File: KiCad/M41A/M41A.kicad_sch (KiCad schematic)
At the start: 18 parts, among them SW1 RotaryEncoder_Switch, SW2 Rifle Fire, SW3 Granade fire, SW4 Cock, SW5 Magazine reload

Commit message: Actrualized KiCad project library.
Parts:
- removed H6: +5V, Connector_PinHeader_1.00mm:PinHeader_1x01_P1.00mm_Vertical, symbol Mechanical:MountingHole_Pad
- removed H7: GND, Connector_PinHeader_1.00mm:PinHeader_1x01_P1.00mm_Vertical, symbol Mechanical:MountingHole_Pad
- added BAT1: 5V, ProjectLibrary:Battery, symbol Device:Battery_Cell
- C1: footprint Capacitor_THT:CP_Axial_L11.0mm_D5.0mm_P18.00mm_Horizontal -> Capacitor_THT:C_Disc_D3.0mm_W2.0mm_P2.50mm
- DFPlayer1: value DFR0299 -> DFPlayer; symbol ByPS_Library:DFR0299 -> Project_Library:DFPlayer
- DRV-74HC595-1: footprint Connector_PinHeader_1.00mm:PinHeader_1x03_P1.00mm_Vertical -> Connector_PinHeader_1.00mm:PinHeader_1x05_P1.00mm_Vertical; symbol ByPS_Library:Driver-74HC595-2 -> Project_Library:Driver-74HC595-2
- LS1: footprint Connector_PinHeader_1.00mm:PinHeader_1x02_P1.00mm_Vertical -> ProjectLibrary:Speaker
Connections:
- net GND: now also SW1.C, BAT1.2 (-); no longer SW1.5 (GND)
- net at DRV-74HC595-1.1 (VCC): now also A1.14 (D11)
- net at DRV-74HC595-1.2 (GND): now also A1.15 (D12)
- net at DRV-74HC595-1.3 (SDD): now also A1.16 (D13)
- net at DRV-74HC595-1.5 (LOAD): now also A1.27 (+5V), D1.2 (A), SW1.S2, BAT1.1 (+)
- net at A1.12 (D9): now also SW1.A; no longer SW1.1 (S1)
- net at A1.13 (D10): now also SW1.B; no longer SW1.2 (S2)
- net at A1.20 (A1): now also SW1.S1; no longer SW1.3 (KEY)
- removed net +5V: A1.27 (+5V), D1.2 (A), DRV-74HC595-1.5 (LOAD), SW1.4 (5V)

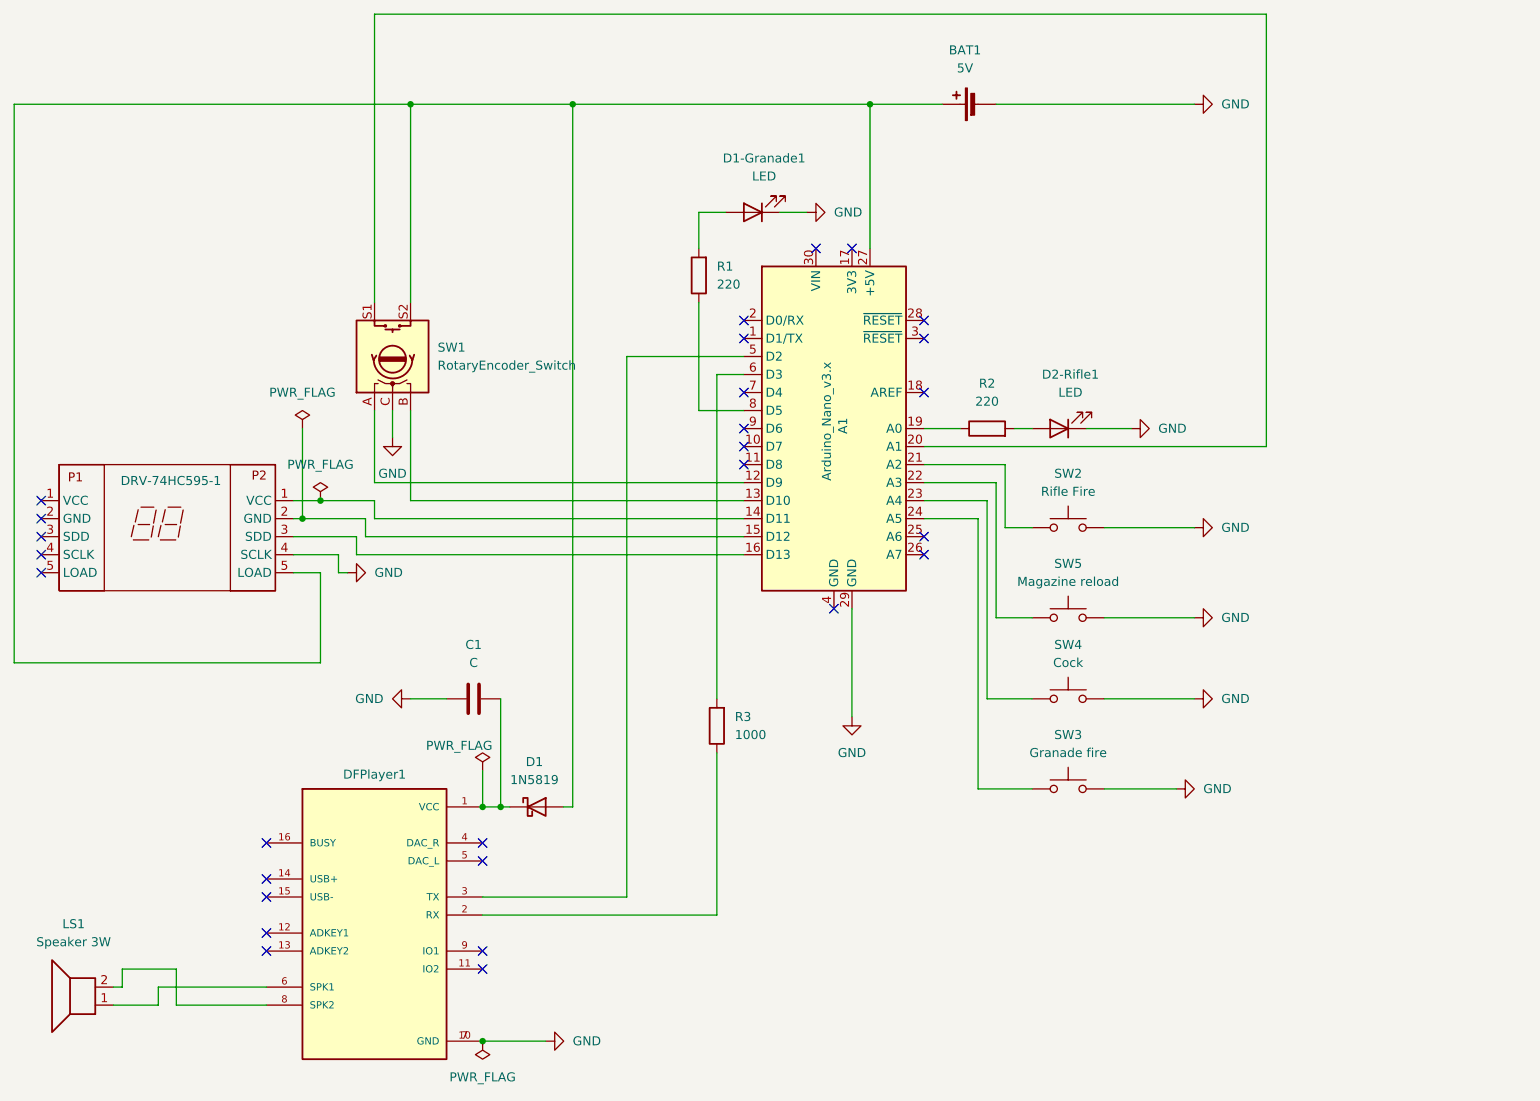
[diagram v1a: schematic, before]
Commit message: Little chage in connection to key pin of rotary encoder.
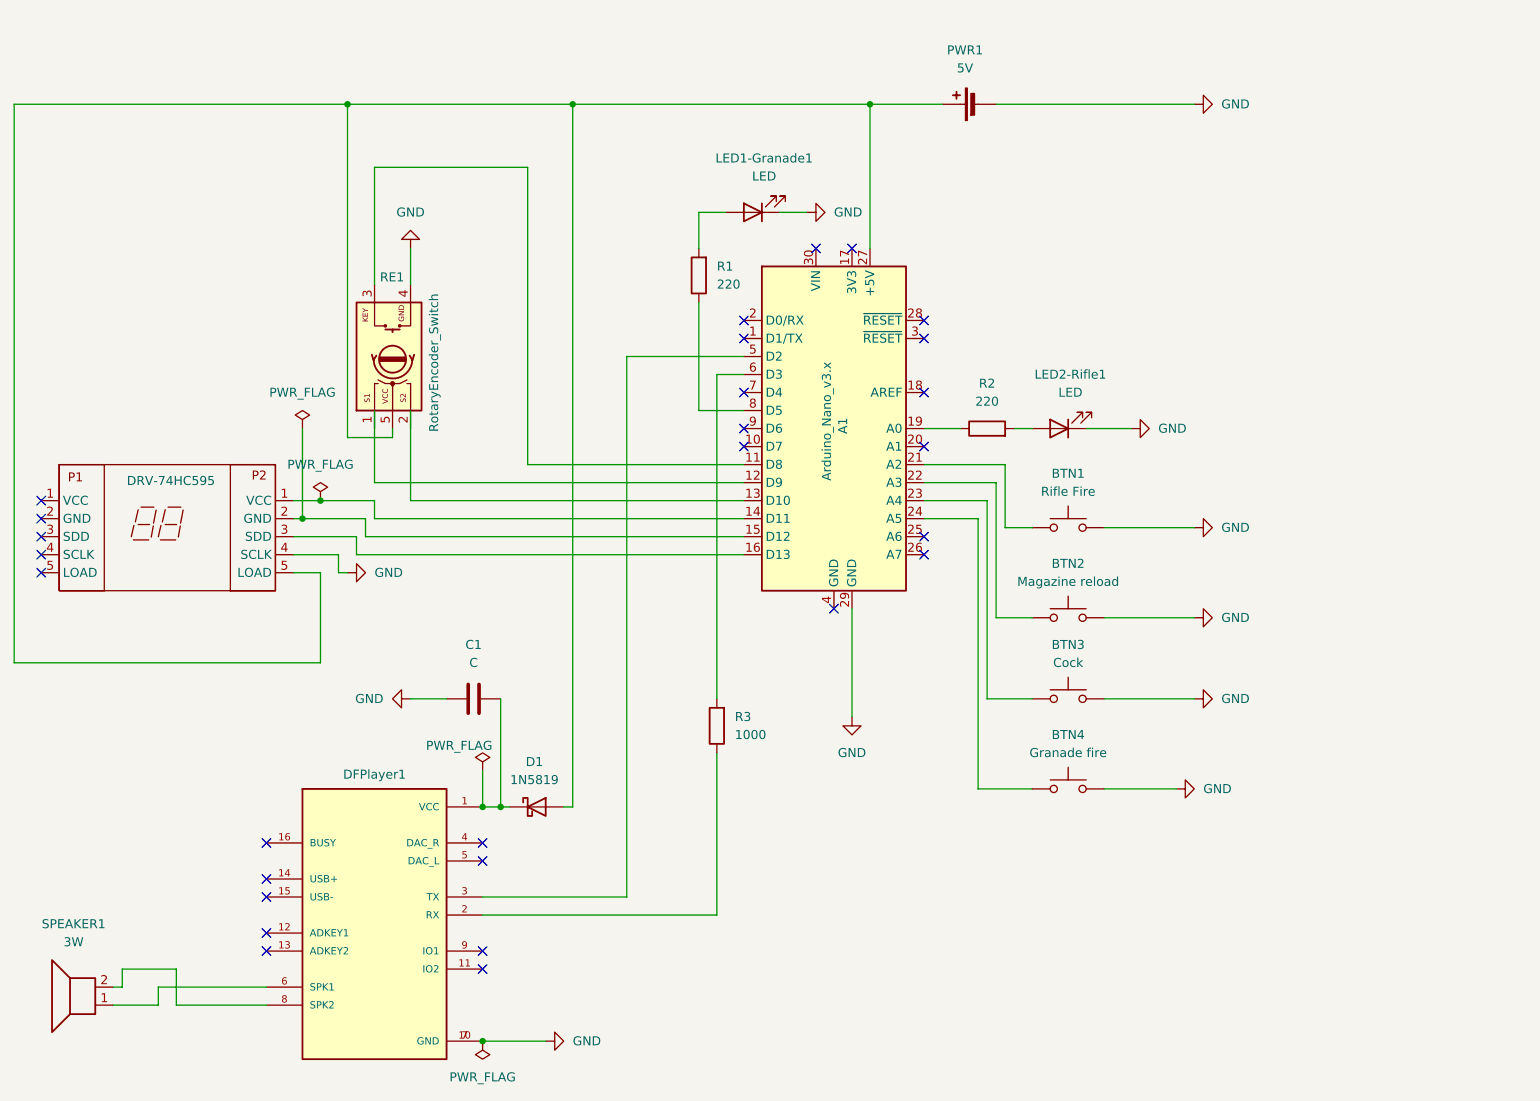
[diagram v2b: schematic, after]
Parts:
- RE1: renamed from SW1; footprint Connector_PinHeader_1.00mm:PinHeader_1x03_P1.00mm_Vertical -> ProjectLibrary:RotaryEncoderLeads; symbol Device:RotaryEncoder_Switch -> Project_Library:RotaryEncoder_Switch
- SPEAKER1: renamed from LS1; value Speaker 3W -> 3W
- renumbered SW2 to BTN1, SW5 to BTN2, SW4 to BTN3, SW3 to BTN4, DRV-74HC595-1 to DRV-74HC595, D1-Granade1 to LED1-Granade1, D2-Rifle1 to LED2-Rifle1, BAT1 to PWR1
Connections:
- net GND: now also RE1.4 (GND); no longer RE1.C
- net at DRV-74HC595.1 (VCC): now also A1.14 (D11)
- net at DRV-74HC595.2 (GND): now also A1.15 (D12)
- net at DRV-74HC595.3 (SDD): now also A1.16 (D13)
- net at DRV-74HC595.5 (LOAD): now also A1.27 (+5V), D1.2 (A), PWR1.1 (+), RE1.5 (VCC)
- net at A1.12 (D9): no longer RE1.A
- net at A1.13 (D10): no longer RE1.B
- net at A1.20 (A1): no longer RE1.S1
- net at A1.11 (D8): now also RE1.3 (KEY)
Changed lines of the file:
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@@
-	)
-	(junction
-		(at 71.12 34.29)
-		(diameter 0)
-		(color 0 0 0 0)
 	)
 	(junction
@@
 	)
 	(junction
+		(at 62.23 34.29)
+		(diameter 0)
+		(color 0 0 0 0)
+	)
+	(junction
 		(at 58.42 90.17)
 		(diameter 0)
@@
 	)
 	(no_connect
+		(at 143.51 82.55)
+	)
+	(no_connect
 		(at 50.8 138.43)
 	)
@@
 	)
 	(no_connect
-		(at 118.11 85.09)
-	)
-	(no_connect
 		(at 128.27 54.61)
 	)
@@
 	(wire
 		(pts
+			(xy 87.63 43.18) (xy 87.63 85.09)
+		)
+		(stroke
+			(width 0)
+			(type default)
+		)
+	)
+	(wire
+		(pts
 			(xy 151.13 130.81) (xy 151.13 92.71)
 		)
@@
 	(wire
 		(pts
+			(xy 62.23 34.29) (xy 93.98 34.29)
+		)
+		(stroke
+			(width 0)
+			(type default)
+		)
+	)
+	(wire
+		(pts
 			(xy 114.3 72.39) (xy 114.3 118.11)
 		)
@@
 	(wire
 		(pts
-			(xy 68.58 77.47) (xy 68.58 81.28)
-		)
-		(stroke
-			(width 0)
-			(type default)
-		)
-	)
-	(wire
-		(pts
 			(xy 63.5 95.25) (xy 54.61 95.25)
 		)
@@
 	(wire
 		(pts
-			(xy 143.51 82.55) (xy 191.77 82.55)
-		)
-		(stroke
-			(width 0)
-			(type default)
-		)
-	)
-	(wire
-		(pts
 			(xy 66.04 77.47) (xy 66.04 87.63)
 		)
@@
 	(wire
 		(pts
-			(xy 66.04 21.59) (xy 191.77 21.59)
+			(xy 66.04 59.69) (xy 66.04 43.18)
 		)
 		(stroke
@@
 	(wire
 		(pts
-			(xy 66.04 21.59) (xy 66.04 62.23)
-		)
-		(stroke
-			(width 0)
-			(type default)
-		)
-	)
-	(wire
-		(pts
-			(xy 15.24 34.29) (xy 71.12 34.29)
+			(xy 15.24 34.29) (xy 62.23 34.29)
 		)
 		(stroke
@@
 	(wire
 		(pts
+			(xy 68.58 80.01) (xy 68.58 81.28)
+		)
+		(stroke
+			(width 0)
+			(type default)
+		)
+	)
+	(wire
+		(pts
 			(xy 154.94 93.98) (xy 158.75 93.98)
 		)
@@
 	(wire
 		(pts
-			(xy 191.77 82.55) (xy 191.77 21.59)
-		)
-		(stroke
-			(width 0)
-			(type default)
-		)
-	)
-	(wire
-		(pts
-			(xy 71.12 34.29) (xy 71.12 62.23)
+			(xy 87.63 85.09) (xy 118.11 85.09)
 		)
 		(stroke
@@
 	(wire
 		(pts
+			(xy 62.23 81.28) (xy 62.23 34.29)
+		)
+		(stroke
+			(width 0)
+			(type default)
+		)
+	)
+	(wire
+		(pts
 			(xy 118.11 69.85) (xy 101.6 69.85)
 		)
@@
 	(wire
 		(pts
-			(xy 71.12 34.29) (xy 93.98 34.29)
-		)
-		(stroke
-			(width 0)
-			(type default)
-		)
-	)
-	(wire
-		(pts
 			(xy 135.89 34.29) (xy 135.89 54.61)
 		)
@@
 	(wire
 		(pts
+			(xy 66.04 43.18) (xy 87.63 43.18)
+		)
+		(stroke
+			(width 0)
+			(type default)
+		)
+	)
+	(wire
+		(pts
 			(xy 168.91 93.98) (xy 181.61 93.98)
 		)
@@
 		(pts
 			(xy 111.76 62.23) (xy 111.76 77.47)
+		)
+		(stroke
+			(width 0)
+			(type default)
+		)
+	)
+	(wire
+		(pts
+			(xy 71.12 54.61) (xy 71.12 59.69)
+		)
+		(stroke
+			(width 0)
+			(type default)
+		)
+	)
+	(wire
+		(pts
+			(xy 68.58 81.28) (xy 62.23 81.28)
 		)
 		(stroke
@@
 		(dnp no)
 		(fields_autoplaced yes)
-		(property "Reference" "SW4"
+		(property "Reference" "BTN3"
 			(at 163.83 110.49 0)
 			(effects
@@
 			(project "M41A"
 				(path "/acff4d07-702e-487a-b98e-cf041378c177"
-					(reference "SW4")
+					(reference "BTN3")
 					(unit 1)
 				)
@@
 		(dnp no)
 		(fields_autoplaced yes)
-		(property "Reference" "LS1"
+		(property "Reference" "SPEAKER1"
 			(at 23.622 149.86 0)
 			(effects
@@
 			)
 		)
-		(property "Value" "Speaker 3W"
+		(property "Value" "3W"
 			(at 23.622 152.4 0)
 			(effects
@@
 			(project "M41A"
 				(path "/acff4d07-702e-487a-b98e-cf041378c177"
-					(reference "LS1")
+					(reference "SPEAKER1")
 					(unit 1)
 				)
@@
 		(on_board yes)
 		(dnp no)
-		(property "Reference" "DRV-74HC595-1"
+		(property "Reference" "DRV-74HC595"
 			(at 37.338 87.376 0)
 			(effects
@@
 			(project "M41A"
 				(path "/acff4d07-702e-487a-b98e-cf041378c177"
-					(reference "DRV-74HC595-1")
+					(reference "DRV-74HC595")
 					(unit 1)
 				)
@@
 	(symbol
 		(lib_id "power:GND")
-		(at 68.58 81.28 0)
+		(at 71.12 54.61 180)
 		(unit 1)
 		(exclude_from_sim no)
@@
 		(fields_autoplaced yes)
 		(property "Reference" "#PWR06"
-			(at 68.58 87.63 0)
+			(at 71.12 48.26 0)
 			(effects
 				(font
@@
 		)
 		(property "Value" "GND"
-			(at 68.58 86.36 0)
+			(at 71.12 49.53 0)
 			(effects
 				(font
@@
 		)
 		(property "Footprint" ""
-			(at 68.58 81.28 0)
+			(at 71.12 54.61 0)
 			(effects
 				(font
@@
 		)
 		(property "Datasheet" ""
-			(at 68.58 81.28 0)
+			(at 71.12 54.61 0)
 			(effects
 				(font
@@
 		)
 		(property "Description" "Power symbol creates a global label with name \"GND\" , ground"
-			(at 68.58 81.28 0)
+			(at 71.12 54.61 0)
 			(effects
 				(font
@@
 		(dnp no)
 		(fields_autoplaced yes)
-		(property "Reference" "D1-Granade1"
+		(property "Reference" "LED1-Granade1"
 			(at 120.9675 41.91 0)
 			(effects
@@
 			(project "M41A"
 				(path "/acff4d07-702e-487a-b98e-cf041378c177"
-					(reference "D1-Granade1")
+					(reference "LED1-Granade1")
 					(unit 1)
 				)
@@
 		(on_board yes)
 		(dnp no)
-		(property "Reference" "SW2"
+		(property "Reference" "BTN1"
 			(at 163.83 86.36 0)
 			(effects
@@
 			(project "M41A"
 				(path "/acff4d07-702e-487a-b98e-cf041378c177"
-					(reference "SW2")
+					(reference "BTN1")
 					(unit 1)
 				)
@@
 	)
 	(symbol
-		(lib_id "Device:RotaryEncoder_Switch")
+		(lib_id "Project_Library:RotaryEncoder_Switch")
 		(at 68.58 69.85 90)
 		(unit 1)
@@
 		(on_board yes)
 		(dnp no)
-		(fields_autoplaced yes)
-		(property "Reference" "SW1"
-			(at 74.93 68.5799 90)
+		(property "Reference" "RE1"
+			(at 66.802 58.674 90)
 			(effects
 				(font
@@
 		)
 		(property "Value" "RotaryEncoder_Switch"
-			(at 74.93 71.1199 90)
+			(at 74.422 60.96 0)
 			(effects
 				(font
@@
 			)
 		)
-		(property "Footprint" "Connector_PinHeader_1.00mm:PinHeader_1x03_P1.00mm_Vertical"
-			(at 58.674 71.628 0)
+		(property "Footprint" "ProjectLibrary:RotaryEncoderLeads"
+			(at 48.768 69.596 0)
 			(effects
 				(font
@@
 		)
 		(property "Description" "Rotary encoder, dual channel, incremental quadrate outputs, with switch"
-			(at 81.026 68.072 0)
-			(effects
-				(font
-					(size 1.27 1.27)
-				)
-				(hide yes)
-			)
-		)
-		(pin "S1"
-		)
-		(pin "C"
-		)
-		(pin "B"
-		)
-		(pin "S2"
-		)
-		(pin "A"
+			(at 87.376 67.31 0)
+			(effects
+				(font
+					(size 1.27 1.27)
+				)
+				(hide yes)
+			)
+		)
+		(pin "4"
+		)
+		(pin "3"
+		)
+		(pin "2"
+		)
+		(pin "5"
+		)
+		(pin "1"
 		)
 		(instances
 			(project "M41A"
 				(path "/acff4d07-702e-487a-b98e-cf041378c177"
-					(reference "SW1")
+					(reference "RE1")
 					(unit 1)
 				)
@@
 		(dnp no)
 		(fields_autoplaced yes)
-		(property "Reference" "D2-Rifle1"
+		(property "Reference" "LED2-Rifle1"
 			(at 164.1475 72.39 0)
 			(effects
@@
 			(project "M41A"
 				(path "/acff4d07-702e-487a-b98e-cf041378c177"
-					(reference "D2-Rifle1")
+					(reference "LED2-Rifle1")
 					(unit 1)
 				)
@@
 		(dnp no)
 		(fields_autoplaced yes)
-		(property "Reference" "BAT1"
+		(property "Reference" "PWR1"
 			(at 149.2885 26.67 90)
 			(effects
@@
 			(project "M41A"
 				(path "/acff4d07-702e-487a-b98e-cf041378c177"
-					(reference "BAT1")
+					(reference "PWR1")
 					(unit 1)
 				)
@@
 		(dnp no)
 		(fields_autoplaced yes)
-		(property "Reference" "SW5"
+		(property "Reference" "BTN2"
 			(at 163.83 99.06 0)
 			(effects
@@
 			(project "M41A"
 				(path "/acff4d07-702e-487a-b98e-cf041378c177"
-					(reference "SW5")
+					(reference "BTN2")
 					(unit 1)
 				)
@@
 		(dnp no)
 		(fields_autoplaced yes)
-		(property "Reference" "SW3"
+		(property "Reference" "BTN4"
 			(at 163.83 123.19 0)
 			(effects
@@
 			(project "M41A"
 				(path "/acff4d07-702e-487a-b98e-cf041378c177"
-					(reference "SW3")
+					(reference "BTN4")
 					(unit 1)
 				)

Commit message: +KiCad schematic files
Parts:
- BTN1, BTN2, BTN3, BTN4: footprint Connector_PinHeader_1.00mm:PinHeader_2x01_P1.00mm_Vertical -> ProjectLibrary:Button Leads 2x 2.54
- DRV-74HC595: footprint Connector_PinHeader_1.00mm:PinHeader_1x05_P1.00mm_Vertical -> ProjectLibrary:Segment Display Leads 5x 2.54
- LED1-Granade1, LED2-Rifle1: footprint Connector_PinHeader_1.00mm:PinHeader_2x01_P1.00mm_Vertical -> ProjectLibrary:LED Leads 2x 2.54
- PWR1: footprint ProjectLibrary:Battery -> ProjectLibrary:Battery 4x 2.54
- RE1: footprint ProjectLibrary:RotaryEncoderLeads -> ProjectLibrary:RotaryEncoder Leads 5x 2.54
- SPEAKER1: footprint ProjectLibrary:Speaker -> ProjectLibrary:Speaker Leads 2x 2.54
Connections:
- net at DRV-74HC595.1 (VCC): now also A1.14 (D11)
- net at DRV-74HC595.2 (GND): now also A1.15 (D12)
- net at DRV-74HC595.3 (SDD): now also A1.16 (D13)
- net at DRV-74HC595.5 (LOAD): now also A1.27 (+5V), D1.2 (A), PWR1.1 (+), RE1.5 (VCC)
- net at RE1.1 (S1): now also A1.12 (D9)
- net at RE1.2 (S2): now also A1.13 (D10)
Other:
- moved on the sheet: RE1
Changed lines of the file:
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@@
+	(wire
+		(pts
+			(xy 66.04 78.74) (xy 66.04 87.63)
+		)
+		(stroke
+			(width 0)
+			(type default)
+		)
+	)
 	(wire
 		(pts
@@
 	(wire
 		(pts
-			(xy 66.04 77.47) (xy 66.04 87.63)
-		)
-		(stroke
-			(width 0)
-			(type default)
-		)
-	)
-	(wire
-		(pts
 			(xy 83.82 118.11) (xy 83.82 133.35)
 		)
@@
 	(wire
 		(pts
-			(xy 66.04 59.69) (xy 66.04 43.18)
+			(xy 66.04 58.42) (xy 66.04 43.18)
 		)
 		(stroke
@@
 	(wire
 		(pts
-			(xy 71.12 77.47) (xy 71.12 90.17)
-		)
-		(stroke
-			(width 0)
-			(type default)
-		)
-	)
-	(wire
-		(pts
 			(xy 154.94 85.09) (xy 154.94 93.98)
 		)
@@
 	(wire
 		(pts
-			(xy 68.58 80.01) (xy 68.58 81.28)
+			(xy 68.58 78.74) (xy 68.58 81.28)
 		)
 		(stroke
@@
 	(wire
 		(pts
+			(xy 71.12 78.74) (xy 71.12 90.17)
+		)
+		(stroke
+			(width 0)
+			(type default)
+		)
+	)
+	(wire
+		(pts
 			(xy 64.77 95.25) (xy 64.77 92.71)
 		)
@@
 	(wire
 		(pts
-			(xy 71.12 54.61) (xy 71.12 59.69)
+			(xy 71.12 54.61) (xy 71.12 58.42)
 		)
 		(stroke
@@
 			)
 		)
-		(property "Footprint" "Connector_PinHeader_1.00mm:PinHeader_2x01_P1.00mm_Vertical"
+		(property "Footprint" "ProjectLibrary:Button Leads 2x 2.54"
 			(at 163.83 113.03 0)
 			(effects
@@
 			)
 		)
-		(property "Footprint" "ProjectLibrary:Speaker"
+		(property "Footprint" "ProjectLibrary:Speaker Leads 2x 2.54"
 			(at 24.13 156.21 0)
 			(effects
@@
 			)
 		)
-		(property "Footprint" "Connector_PinHeader_1.00mm:PinHeader_1x05_P1.00mm_Vertical"
+		(property "Footprint" "ProjectLibrary:Segment Display Leads 5x 2.54"
 			(at 36.83 77.216 0)
 			(effects
@@
 			)
 		)
-		(property "Footprint" "Connector_PinHeader_1.00mm:PinHeader_2x01_P1.00mm_Vertical"
+		(property "Footprint" "ProjectLibrary:LED Leads 2x 2.54"
 			(at 119.38 49.53 0)
 			(effects
@@
 			)
 		)
-		(property "Footprint" "Connector_PinHeader_1.00mm:PinHeader_2x01_P1.00mm_Vertical"
+		(property "Footprint" "ProjectLibrary:Button Leads 2x 2.54"
 			(at 163.83 88.9 0)
 			(effects
@@
 	(symbol
 		(lib_id "Project_Library:RotaryEncoder_Switch")
-		(at 68.58 69.85 90)
+		(at 68.58 68.58 90)
 		(unit 1)
 		(exclude_from_sim no)
@@
 		(dnp no)
 		(property "Reference" "RE1"
-			(at 66.802 58.674 90)
+			(at 66.802 57.404 90)
 			(effects
 				(font
@@
 		)
 		(property "Value" "RotaryEncoder_Switch"
-			(at 74.422 60.96 0)
+			(at 74.422 59.69 0)
 			(effects
 				(font
@@
 			)
 		)
-		(property "Footprint" "ProjectLibrary:RotaryEncoderLeads"
-			(at 48.768 69.596 0)
+		(property "Footprint" "ProjectLibrary:RotaryEncoder Leads 5x 2.54"
+			(at 48.768 68.326 0)
 			(effects
 				(font
@@
 		)
 		(property "Datasheet" "~"
-			(at 61.976 69.85 0)
+			(at 61.976 68.58 0)
 			(effects
 				(font
@@
 		)
 		(property "Description" "Rotary encoder, dual channel, incremental quadrate outputs, with switch"
-			(at 87.376 67.31 0)
+			(at 87.376 66.04 0)
 			(effects
 				(font
@@
 			)
 		)
-		(property "Footprint" "Connector_PinHeader_1.00mm:PinHeader_2x01_P1.00mm_Vertical"
+		(property "Footprint" "ProjectLibrary:LED Leads 2x 2.54"
 			(at 162.56 80.01 0)
 			(effects
@@
 			)
 		)
-		(property "Footprint" "ProjectLibrary:Battery"
+		(property "Footprint" "ProjectLibrary:Battery 4x 2.54"
 			(at 149.606 34.29 90)
 			(effects
@@
 			)
 		)
-		(property "Footprint" "Connector_PinHeader_1.00mm:PinHeader_2x01_P1.00mm_Vertical"
+		(property "Footprint" "ProjectLibrary:Button Leads 2x 2.54"
 			(at 163.83 101.6 0)
 			(effects
@@
 			)
 		)
-		(property "Footprint" "Connector_PinHeader_1.00mm:PinHeader_2x01_P1.00mm_Vertical"
+		(property "Footprint" "ProjectLibrary:Button Leads 2x 2.54"
 			(at 163.83 125.73 0)
 			(effects

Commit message: Actualized schema
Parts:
- added C1: 100 µF, Capacitor_THT:CP_Radial_D5.0mm_P2.50mm, symbol Device:C_Polarized
- added C2, C4: 100 nF, Capacitor_THT:C_Rect_L4.0mm_W2.5mm_P2.50mm, symbol Device:C
- added D1: 1N5819, Diode_THT:D_DO-41_SOD81_P10.16mm_Horizontal, symbol Diode:1N5819
- added SW1: SW_PWR_ON_OFF, Button_Switch_THT:SW_DIP_SPSTx01_Piano_10.8x4.1mm_W7.62mm_P2.54mm, symbol Switch:SW_SPST
- C3: renamed from C1; value C -> 2000 µF; symbol Device:C -> Device:C_Polarized
- renumbered D1 to D2
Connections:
- net GND: now also DRV-74HC595.2 (GND), C1.2, C2.2, C4.1; no longer DRV-74HC595.4 (SCLK)
- net at DRV-74HC595.1 (VCC): now also A1.27 (+5V), D2.2 (A), RE1.5 (VCC), C1.1, C2.1, D1.1 (K)
- net at A1.14 (D11): now also DRV-74HC595.4 (SCLK); no longer DRV-74HC595.1 (VCC)
- net at A1.15 (D12): now also DRV-74HC595.5 (LOAD); no longer DRV-74HC595.2 (GND)
- net at DRV-74HC595.3 (SDD): now also A1.16 (D13)
- net at C3.1, D2.1 (K), DFPlayer1.1 (VCC): now also C4.2
- new net: D1.2 (A), SW1.1 (A)
- new net: PWR1.1 (+), SW1.2 (B)
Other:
- moved on the sheet: D2, LED1-Granade1, PWR1, R1
